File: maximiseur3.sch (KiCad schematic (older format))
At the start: 38 parts, among them J1 PV+/M+, J2 M-, J3 PV-, P1 SW SW, Q1 IRLB3036G, Q2 IRLB3036G, Q3 IRLB3036G, Q4 IRLB3036G, T1 BD139, U1 LM311

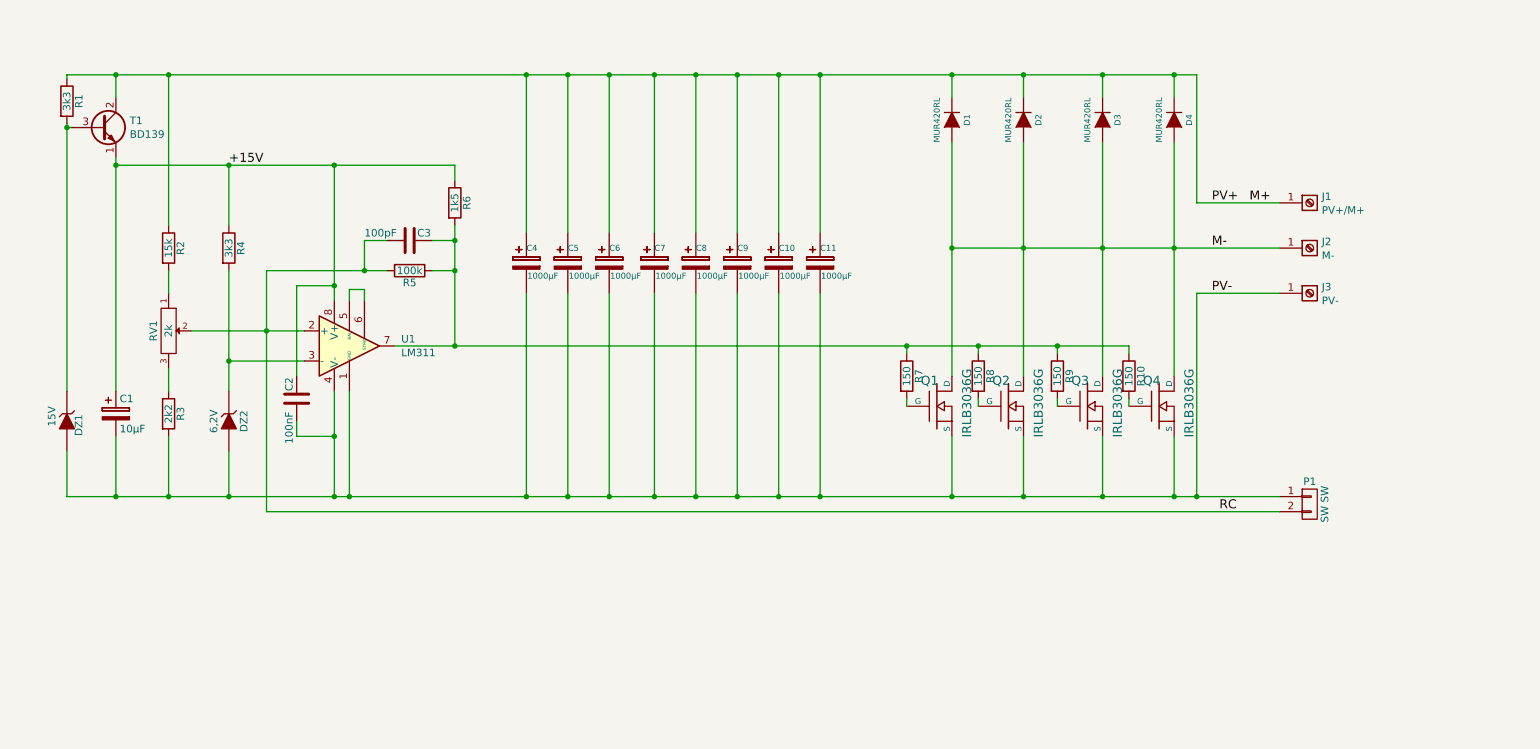
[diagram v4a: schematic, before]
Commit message: ajout de varistances de protection, taille définitive du PCB
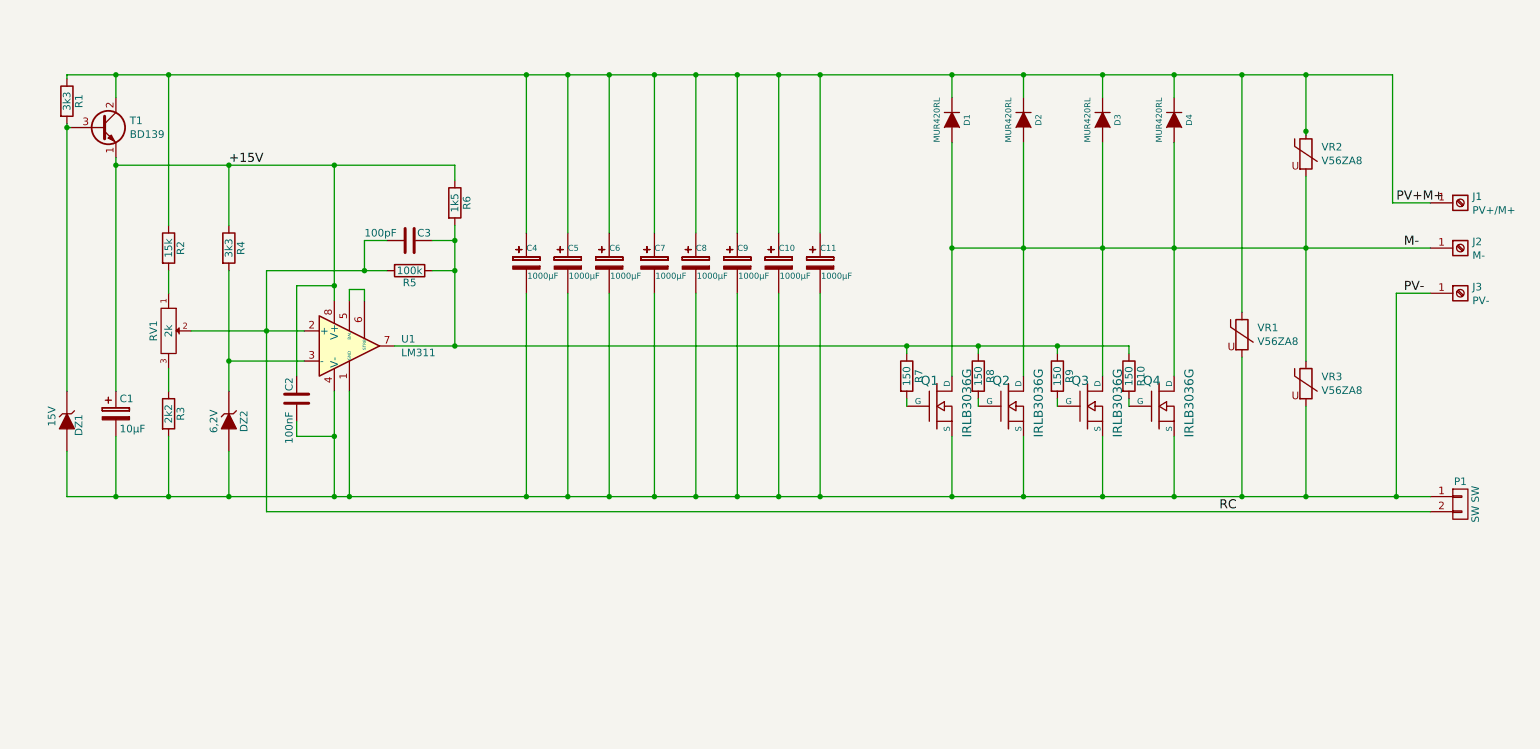
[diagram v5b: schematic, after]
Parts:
- added VR1, VR2, VR3: V56ZA8, Varistor:RV_Disc_D15.5mm_W4.5mm_P7.5mm, symbol Device:Varistor
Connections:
- net M+: now also VR1.1, VR2.1
- net M-: now also VR2.2, VR3.1
- net PV-: now also VR1.2, VR3.2
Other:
- moved on the sheet: J1, J2, J3, P1
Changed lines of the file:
@@
 L maximiseur3-rescue:CONN_01X02 P1
 U 1 1 55B1FA9C
-P 9375 4150
-F 0 "P1" H 9375 4300 50  0000 C CNN
-F 1 "SW   SW" V 9475 4150 50  0000 C CNN
-F 2 "maximiseur:bornier2" H 9375 4150 60  0001 C CNN
-F 3 "" H 9375 4150 60  0000 C CNN
-	1    9375 4150
+P 10375 4150
+F 0 "P1" H 10375 4300 50  0000 C CNN
+F 1 "SW   SW" V 10475 4150 50  0000 C CNN
+F 2 "maximiseur:bornier2" H 10375 4150 60  0001 C CNN
+F 3 "" H 10375 4150 60  0000 C CNN
+	1    10375 4150
 	1    0    0    -1
 $EndComp
@@
 	2450 2600 3100 2600
 Connection ~ 2900 4100
-Connection ~ 8625 4100
-Text Label 8725 2750 0    60   ~ 0
+Text Label 10000 2750 0    60   ~ 0
 PV-
-Text Label 8725 2150 0    60   ~ 0
+Text Label 9950 2150 0    60   ~ 0
 PV+
-Text Label 8725 2450 0    60   ~ 0
+Text Label 10000 2450 0    60   ~ 0
 M-
 Text Label 8775 4200 0    60   ~ 0
 RC
-Text Label 8975 2150 0    60   ~ 0
+Text Label 10125 2150 0    60   ~ 0
 M+
 Text Label 2200 1900 0    60   ~ 0
 +15V
-Wire Wire Line
-	9175 2150 8625 2150
-Wire Wire Line
-	8625 1300 8625 2150
-Wire Wire Line
-	9175 2450 8475 2450
 Connection ~ 7475 2450
 Wire Wire Line
@@
 Wire Wire Line
 	7475 4100 8000 4100
-Wire Wire Line
-	8625 4100 9175 4100
 Wire Wire Line
 	7475 2450 7475 3300
@@
 Connection ~ 8475 4100
 Wire Wire Line
-	8475 4100 8625 4100
-Wire Wire Line
 	8000 3300 8000 2450
 Connection ~ 8000 2450
@@
 Wire Wire Line
 	4450 4100 4725 4100
-Wire Wire Line
-	2450 4200 9175 4200
 Wire Wire Line
 	3700 3100 3700 2600
@@
 $EndComp
 Connection ~ 8475 1300
-Wire Wire Line
-	8475 1300 8625 1300
 $Comp
 L maximiseur3-rescue:LM311-Comparator U1
@@
 L screw_terminal_01x01:Screw_Terminal_01x01 J1
 U 1 1 5D4F4A74
-P 9375 2150
-F 0 "J1" H 9455 2192 50  0000 L CNN
-F 1 "PV+/M+" H 9455 2101 50  0000 L CNN
-F 2 "maximiseur:7808" H 9375 2150 50  0001 C CNN
-F 3 "~" H 9375 2150 50  0001 C CNN
-	1    9375 2150
+P 10375 2150
+F 0 "J1" H 10455 2192 50  0000 L CNN
+F 1 "PV+/M+" H 10455 2101 50  0000 L CNN
+F 2 "maximiseur:7808" H 10375 2150 50  0001 C CNN
+F 3 "~" H 10375 2150 50  0001 C CNN
+	1    10375 2150
 	1    0    0    -1
 $EndComp
@@
 L screw_terminal_01x01:Screw_Terminal_01x01 J3
 U 1 1 5D4F96DA
-P 9375 2750
-F 0 "J3" H 9455 2792 50  0000 L CNN
-F 1 "PV-" H 9455 2701 50  0000 L CNN
-F 2 "maximiseur:7808" H 9375 2750 50  0001 C CNN
-F 3 "~" H 9375 2750 50  0001 C CNN
-	1    9375 2750
+P 10375 2750
+F 0 "J3" H 10455 2792 50  0000 L CNN
+F 1 "PV-" H 10455 2701 50  0000 L CNN
+F 2 "maximiseur:7808" H 10375 2750 50  0001 C CNN
+F 3 "~" H 10375 2750 50  0001 C CNN
+	1    10375 2750
 	1    0    0    -1
 $EndComp
@@
 L screw_terminal_01x01:Screw_Terminal_01x01 J2
 U 1 1 5D4F992A
-P 9375 2450
-F 0 "J2" H 9455 2492 50  0000 L CNN
-F 1 "M-" H 9455 2401 50  0000 L CNN
-F 2 "maximiseur:7808" H 9375 2450 50  0001 C CNN
-F 3 "~" H 9375 2450 50  0001 C CNN
-	1    9375 2450
-	1    0    0    -1
-$EndComp
-Wire Wire Line
-	9175 2750 8625 2750
-Wire Wire Line
-	8625 2750 8625 4100
+P 10375 2450
+F 0 "J2" H 10455 2492 50  0000 L CNN
+F 1 "M-" H 10455 2401 50  0000 L CNN
+F 2 "maximiseur:7808" H 10375 2450 50  0001 C CNN
+F 3 "~" H 10375 2450 50  0001 C CNN
+	1    10375 2450
+	1    0    0    -1
+$EndComp
 Connection ~ 6700 3100
 Connection ~ 3700 3100
@@
 Wire Wire Line
 	2900 3700 2900 4100
+$Comp
+L Device:Varistor VR1
+U 1 1 5D5E3C76
+P 8925 3025
+F 0 "VR1" H 9028 3071 50  0000 L CNN
+F 1 "V56ZA8" H 9028 2980 50  0000 L CNN
+F 2 "Varistor:RV_Disc_D15.5mm_W4.5mm_P7.5mm" V 8855 3025 50  0001 C CNN
+F 3 "~" H 8925 3025 50  0001 C CNN
+	1    8925 3025
+	1    0    0    -1
+$EndComp
+Wire Wire Line
+	8475 2450 9350 2450
+Wire Wire Line
+	8475 4100 8925 4100
+Wire Wire Line
+	9950 2750 9950 4100
+Wire Wire Line
+	9950 2750 10175 2750
+Connection ~ 9950 4100
+Wire Wire Line
+	9950 4100 10175 4100
+Wire Wire Line
+	9925 2150 9925 1300
+Wire Wire Line
+	9925 2150 10175 2150
+Wire Wire Line
+	8475 1300 8925 1300
+Wire Wire Line
+	8925 2875 8925 1300
+Connection ~ 8925 1300
+Wire Wire Line
+	8925 3175 8925 4100
+Connection ~ 8925 4100
+$Comp
+L Device:Varistor VR3
+U 1 1 5D637E14
+P 9350 3350
+F 0 "VR3" H 9453 3396 50  0000 L CNN
+F 1 "V56ZA8" H 9453 3305 50  0000 L CNN
+F 2 "Varistor:RV_Disc_D15.5mm_W4.5mm_P7.5mm" V 9280 3350 50  0001 C CNN
+F 3 "~" H 9350 3350 50  0001 C CNN
+	1    9350 3350
+	1    0    0    -1
+$EndComp
+$Comp
+L Device:Varistor VR2
+U 1 1 5D638AFE
+P 9350 1825
+F 0 "VR2" H 9453 1871 50  0000 L CNN
+F 1 "V56ZA8" H 9453 1780 50  0000 L CNN
+F 2 "Varistor:RV_Disc_D15.5mm_W4.5mm_P7.5mm" V 9280 1825 50  0001 C CNN
+F 3 "~" H 9350 1825 50  0001 C CNN
+	1    9350 1825
+	1    0    0    -1
+$EndComp
+Wire Wire Line
+	9350 1700 9350 1675
+Wire Wire Line
+	8925 1300 9350 1300
+Connection ~ 9350 1300
+Wire Wire Line
+	9350 1300 9925 1300
+Connection ~ 9350 1675
+Wire Wire Line
+	9350 1675 9350 1300
+Wire Wire Line
+	9350 1975 9350 2450
+Connection ~ 9350 2450
+Wire Wire Line
+	9350 2450 10175 2450
+Wire Wire Line
+	9350 2450 9350 3200
+Wire Wire Line
+	9350 3500 9350 4100
+Wire Wire Line
+	8925 4100 9350 4100
+Connection ~ 9350 4100
+Wire Wire Line
+	9350 4100 9950 4100
+Wire Wire Line
+	2450 4200 10175 4200
 $EndSCHEMATC

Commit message: modification PCB : trous de fixation + un peu de ménage
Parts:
- added H1, H2, H3, H4: MountingHole, MountingHole:MountingHole_4.3mm_M4, symbol Mechanical:MountingHole
- VR1, VR2, VR3: symbol Device:Varistor -> maximiseur3-rescue:Varistor-Device
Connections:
- net PV-: now also P1.2 (P2); no longer P1.1 (P1)
- net RC: now also P1.1 (P1); no longer P1.2 (P2)
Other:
- moved on the sheet: C1, C10, C11, C2, C3, C4, C5, C6, C7, C8, C9, D1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

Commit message: derniers ajustements sur serigraphie avant export
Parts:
- C1: footprint Capacitor_THT:CP_Radial_D5.0mm_P2.50mm -> maximiseur:CP_Radial_D5.0mm_P2.50mm
- C2, C3: footprint Capacitor_THT:C_Rect_L7.0mm_W2.0mm_P5.00mm -> maximiseur:C_Rect_L7.0mm_W2.0mm_P5.00mm
- DZ1: value 15V -> 12V; footprint Diode_THT:D_DO-34_SOD68_P7.62mm_Horizontal -> maximiseur:D_DO-34_SOD68_P7.62mm_Horizontal
- DZ2: footprint Diode_THT:D_DO-34_SOD68_P7.62mm_Horizontal -> maximiseur:D_DO-34_SOD68_P7.62mm_Horizontal
- H1, H2, H3, H4: footprint MountingHole:MountingHole_4.3mm_M4 -> maximiseur:MountingHole_4.3mm_M4
- R1, R10, R2, R3, R4, R5, R6, R7, R8, R9: footprint Resistor_THT:R_Axial_DIN0207_L6.3mm_D2.5mm_P10.16mm_Horizontal -> maximiseur:R_Axial_DIN0207_L6.3mm_D2.5mm_P10.16mm_Horizontal
- T1: footprint Package_TO_SOT_THT:TO-126-3_Vertical -> maximiseur:TO-126-3_Vertical
- U1: footprint Package_DIP:DIP-8_W7.62mm_LongPads -> maximiseur:DIP-8_W7.62mm_LongPads
- VR1, VR2, VR3: footprint Varistor:RV_Disc_D15.5mm_W4.5mm_P7.5mm -> maximiseur:RV_Disc_D15.5mm_W4.5mm_P7.5mm
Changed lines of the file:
@@
 F 0 "R2" V 1880 2050 50  0000 C CNN
 F 1 "15k" V 1800 2050 50  0000 C CNN
-F 2 "Resistor_THT:R_Axial_DIN0207_L6.3mm_D2.5mm_P10.16mm_Horizontal" V 1730 2050 30  0001 C CNN
+F 2 "maximiseur:R_Axial_DIN0207_L6.3mm_D2.5mm_P10.16mm_Horizontal" V 1730 2050 30  0001 C CNN
 F 3 "" H 1800 2050 30  0000 C CNN
 	1    1800 2050
@@
 F 0 "R3" V 1880 3150 50  0000 C CNN
 F 1 "2k2" V 1800 3150 50  0000 C CNN
-F 2 "Resistor_THT:R_Axial_DIN0207_L6.3mm_D2.5mm_P10.16mm_Horizontal" V 1730 3150 30  0001 C CNN
+F 2 "maximiseur:R_Axial_DIN0207_L6.3mm_D2.5mm_P10.16mm_Horizontal" V 1730 3150 30  0001 C CNN
 F 3 "" H 1800 3150 30  0000 C CNN
 	1    1800 3150
@@
 F 0 "R4" V 2280 2050 50  0000 C CNN
 F 1 "3k3" V 2200 2050 50  0000 C CNN
-F 2 "Resistor_THT:R_Axial_DIN0207_L6.3mm_D2.5mm_P10.16mm_Horizontal" V 2130 2050 30  0001 C CNN
+F 2 "maximiseur:R_Axial_DIN0207_L6.3mm_D2.5mm_P10.16mm_Horizontal" V 2130 2050 30  0001 C CNN
 F 3 "" H 2200 2050 30  0000 C CNN
 	1    2200 2050
@@
 F 0 "R6" V 3780 1750 50  0000 C CNN
 F 1 "1k5" V 3700 1750 50  0000 C CNN
-F 2 "Resistor_THT:R_Axial_DIN0207_L6.3mm_D2.5mm_P10.16mm_Horizontal" V 3630 1750 30  0001 C CNN
+F 2 "maximiseur:R_Axial_DIN0207_L6.3mm_D2.5mm_P10.16mm_Horizontal" V 3630 1750 30  0001 C CNN
 F 3 "" H 3700 1750 30  0000 C CNN
 	1    3700 1750
@@
 F 0 "R5" V 3480 2200 50  0000 C CNN
 F 1 "100k" V 3400 2200 50  0000 C CNN
-F 2 "Resistor_THT:R_Axial_DIN0207_L6.3mm_D2.5mm_P10.16mm_Horizontal" V 3330 2200 30  0001 C CNN
+F 2 "maximiseur:R_Axial_DIN0207_L6.3mm_D2.5mm_P10.16mm_Horizontal" V 3330 2200 30  0001 C CNN
 F 3 "" H 3400 2200 30  0000 C CNN
 	1    3400 2200
@@
 F 0 "C3" V 3350 2050 50  0000 L CNN
 F 1 "100pF" V 3350 1700 50  0000 L CNN
-F 2 "Capacitor_THT:C_Rect_L7.0mm_W2.0mm_P5.00mm" H 3438 1850 30  0001 C CNN
+F 2 "maximiseur:C_Rect_L7.0mm_W2.0mm_P5.00mm" H 3438 1850 30  0001 C CNN
 F 3 "" H 3400 2000 60  0000 C CNN
 	1    3400 2000
@@
 F 0 "DZ2" H 2200 3300 50  0000 C CNN
 F 1 "6,2V" H 2200 3100 50  0000 C CNN
-F 2 "Diode_THT:D_DO-34_SOD68_P7.62mm_Horizontal" H 2200 3200 60  0001 C CNN
+F 2 "maximiseur:D_DO-34_SOD68_P7.62mm_Horizontal" H 2200 3200 60  0001 C CNN
 F 3 "" H 2200 3200 60  0000 C CNN
 	1    2200 3200
@@
 P 1125 3200
 F 0 "DZ1" H 1079 3279 50  0000 L CNN
-F 1 "15V" H 1025 3100 50  0000 L CNN
-F 2 "Diode_THT:D_DO-34_SOD68_P7.62mm_Horizontal" H 1125 3200 60  0001 C CNN
+F 1 "12V" H 1025 3100 50  0000 L CNN
+F 2 "maximiseur:D_DO-34_SOD68_P7.62mm_Horizontal" H 1125 3200 60  0001 C CNN
 F 3 "" H 1125 3200 60  0000 C CNN
 	1    1125 3200
@@
 F 0 "R1" V 1205 1075 50  0000 C CNN
 F 1 "3k3" V 1125 1075 50  0000 C CNN
-F 2 "Resistor_THT:R_Axial_DIN0207_L6.3mm_D2.5mm_P10.16mm_Horizontal" V 1055 1075 30  0001 C CNN
+F 2 "maximiseur:R_Axial_DIN0207_L6.3mm_D2.5mm_P10.16mm_Horizontal" V 1055 1075 30  0001 C CNN
 F 3 "" H 1125 1075 30  0000 C CNN
 	1    1125 1075
@@
 F 0 "T1" H 1542 1296 50  0000 L CNN
 F 1 "BD139" H 1542 1205 50  0000 L CNN
-F 2 "Package_TO_SOT_THT:TO-126-3_Vertical" H 1550 1175 50  0001 L CIN
+F 2 "maximiseur:TO-126-3_Vertical" H 1550 1175 50  0001 L CIN
 F 3 "http://www.st.com/internet/com/TECHNICAL_RESOURCES/TECHNICAL_LITERATURE/DATASHEET/CD00001225.pdf" H 1350 1250 50  0001 L CNN
 	1    1350 1250
@@
 F 0 "R7" V 6780 2900 50  0000 C CNN
 F 1 "150" V 6700 2900 50  0000 C CNN
-F 2 "Resistor_THT:R_Axial_DIN0207_L6.3mm_D2.5mm_P10.16mm_Horizontal" V 6630 2900 30  0001 C CNN
+F 2 "maximiseur:R_Axial_DIN0207_L6.3mm_D2.5mm_P10.16mm_Horizontal" V 6630 2900 30  0001 C CNN
 F 3 "" H 6700 2900 30  0000 C CNN
 	1    6700 2900
@@
 F 0 "R8" V 7255 2900 50  0000 C CNN
 F 1 "150" V 7175 2900 50  0000 C CNN
-F 2 "Resistor_THT:R_Axial_DIN0207_L6.3mm_D2.5mm_P10.16mm_Horizontal" V 7105 2900 30  0001 C CNN
+F 2 "maximiseur:R_Axial_DIN0207_L6.3mm_D2.5mm_P10.16mm_Horizontal" V 7105 2900 30  0001 C CNN
 F 3 "" H 7175 2900 30  0000 C CNN
 	1    7175 2900
@@
 F 0 "R9" V 7780 2900 50  0000 C CNN
 F 1 "150" V 7700 2900 50  0000 C CNN
-F 2 "Resistor_THT:R_Axial_DIN0207_L6.3mm_D2.5mm_P10.16mm_Horizontal" V 7630 2900 30  0001 C CNN
+F 2 "maximiseur:R_Axial_DIN0207_L6.3mm_D2.5mm_P10.16mm_Horizontal" V 7630 2900 30  0001 C CNN
 F 3 "" H 7700 2900 30  0000 C CNN
 	1    7700 2900
@@
 F 0 "R10" V 8255 2900 50  0000 C CNN
 F 1 "150" V 8175 2900 50  0000 C CNN
-F 2 "Resistor_THT:R_Axial_DIN0207_L6.3mm_D2.5mm_P10.16mm_Horizontal" V 8105 2900 30  0001 C CNN
+F 2 "maximiseur:R_Axial_DIN0207_L6.3mm_D2.5mm_P10.16mm_Horizontal" V 8105 2900 30  0001 C CNN
 F 3 "" H 8175 2900 30  0000 C CNN
 	1    8175 2900
@@
 F 0 "U1" H 3344 2746 50  0000 L CNN
 F 1 "LM311" H 3344 2655 50  0000 L CNN
-F 2 "Package_DIP:DIP-8_W7.62mm_LongPads" H 3000 2700 50  0001 C CNN
+F 2 "maximiseur:DIP-8_W7.62mm_LongPads" H 3000 2700 50  0001 C CNN
 F 3 "http://www.ti.com/lit/ds/symlink/lm311.pdf" H 3000 2700 50  0001 C CNN
 	1    3000 2700
@@
 F 0 "C1" H 1475 3250 50  0000 L CNN
 F 1 "10µF" H 1475 3050 50  0000 L CNN
-F 2 "Capacitor_THT:CP_Radial_D5.0mm_P2.50mm" H 1488 3000 30  0001 C CNN
+F 2 "maximiseur:CP_Radial_D5.0mm_P2.50mm" H 1488 3000 30  0001 C CNN
 F 3 "" H 1450 3150 60  0000 C CNN
 	1    1450 3150
@@
 F 0 "C2" V 2600 3100 50  0000 L CNN
 F 1 "100nF" V 2600 2750 50  0000 L CNN
-F 2 "Capacitor_THT:C_Rect_L7.0mm_W2.0mm_P5.00mm" H 2688 2900 30  0001 C CNN
+F 2 "maximiseur:C_Rect_L7.0mm_W2.0mm_P5.00mm" H 2688 2900 30  0001 C CNN
 F 3 "" H 2650 3050 60  0000 C CNN
 	1    2650 3050
@@
 F 0 "VR1" H 9028 2671 50  0000 L CNN
 F 1 "V56ZA8" H 9028 2580 50  0000 L CNN
-F 2 "Varistor:RV_Disc_D15.5mm_W4.5mm_P7.5mm" V 8855 2625 50  0001 C CNN
+F 2 "maximiseur:RV_Disc_D15.5mm_W4.5mm_P7.5mm" V 8855 2625 50  0001 C CNN
 F 3 "~" H 8925 2625 50  0001 C CNN
 	1    8925 2625
@@
 F 0 "VR3" H 9453 2996 50  0000 L CNN
 F 1 "V56ZA8" H 9453 2905 50  0000 L CNN
-F 2 "Varistor:RV_Disc_D15.5mm_W4.5mm_P7.5mm" V 9280 2950 50  0001 C CNN
+F 2 "maximiseur:RV_Disc_D15.5mm_W4.5mm_P7.5mm" V 9280 2950 50  0001 C CNN
 F 3 "~" H 9350 2950 50  0001 C CNN
 	1    9350 2950
@@
 F 0 "VR2" H 9453 1471 50  0000 L CNN
 F 1 "V56ZA8" H 9453 1380 50  0000 L CNN
-F 2 "Varistor:RV_Disc_D15.5mm_W4.5mm_P7.5mm" V 9280 1425 50  0001 C CNN
+F 2 "maximiseur:RV_Disc_D15.5mm_W4.5mm_P7.5mm" V 9280 1425 50  0001 C CNN
 F 3 "~" H 9350 1425 50  0001 C CNN
 	1    9350 1425
@@
 F 0 "H1" H 1400 5046 50  0000 L CNN
 F 1 "MountingHole" H 1400 4955 50  0000 L CNN
-F 2 "MountingHole:MountingHole_4.3mm_M4" H 1300 5000 50  0001 C CNN
+F 2 "maximiseur:MountingHole_4.3mm_M4" H 1300 5000 50  0001 C CNN
 F 3 "~" H 1300 5000 50  0001 C CNN
 	1    1300 5000
@@
 F 0 "H2" H 1400 5246 50  0000 L CNN
 F 1 "MountingHole" H 1400 5155 50  0000 L CNN
-F 2 "MountingHole:MountingHole_4.3mm_M4" H 1300 5200 50  0001 C CNN
+F 2 "maximiseur:MountingHole_4.3mm_M4" H 1300 5200 50  0001 C CNN
 F 3 "~" H 1300 5200 50  0001 C CNN
 	1    1300 5200
@@
 F 0 "H3" H 1400 5446 50  0000 L CNN
 F 1 "MountingHole" H 1400 5355 50  0000 L CNN
-F 2 "MountingHole:MountingHole_4.3mm_M4" H 1300 5400 50  0001 C CNN
+F 2 "maximiseur:MountingHole_4.3mm_M4" H 1300 5400 50  0001 C CNN
 F 3 "~" H 1300 5400 50  0001 C CNN
 	1    1300 5400
@@
 F 0 "H4" H 1400 5646 50  0000 L CNN
 F 1 "MountingHole" H 1400 5555 50  0000 L CNN
-F 2 "MountingHole:MountingHole_4.3mm_M4" H 1300 5600 50  0001 C CNN
+F 2 "maximiseur:MountingHole_4.3mm_M4" H 1300 5600 50  0001 C CNN
 F 3 "~" H 1300 5600 50  0001 C CNN
 	1    1300 5600

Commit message: ajout seconde empreinte pour le potentiomètre + pads plus larges + sérigraphie
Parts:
- added Rv1: 2k, maximiseur:pot_vert_Radiohm, symbol maximiseur3-rescue:POT
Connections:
- net RC: now also Rv1.2
- net at R2.2: now also RV1.3, Rv1.3; no longer RV1.1
- net at R3.1: now also RV1.1, Rv1.1; no longer RV1.3
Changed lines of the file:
@@
 F 3 "" H 1800 2600 60  0000 C CNN
 	1    1800 2600
-	0    1    1    0
+	0    1    -1   0
 $EndComp
 $Comp
@@
 	1    0    0    -1
 $EndComp
+$Comp
+L maximiseur3-rescue:POT Rv1
+U 1 1 5D5EA3EE
+P 1800 2600
+F 0 "Rv1" H 1750 2425 50  0000 C CNN
+F 1 "2k" H 1800 2600 50  0000 C CNN
+F 2 "maximiseur:pot_vert_Radiohm" H 1800 2600 60  0001 C CNN
+F 3 "" H 1800 2600 60  0000 C CNN
+	1    1800 2600
+	0    1    -1   0
+$EndComp
+Connection ~ 1800 2850
+Connection ~ 1950 2600
+Connection ~ 1800 2350
 $EndSCHEMATC
